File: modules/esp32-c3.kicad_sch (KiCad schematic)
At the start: 26 parts, among them J1 UART0, SW1 BOOT, SW2 RST, U2 ESP32-C3, U3 W25X40CLSN, Y1 40MHz

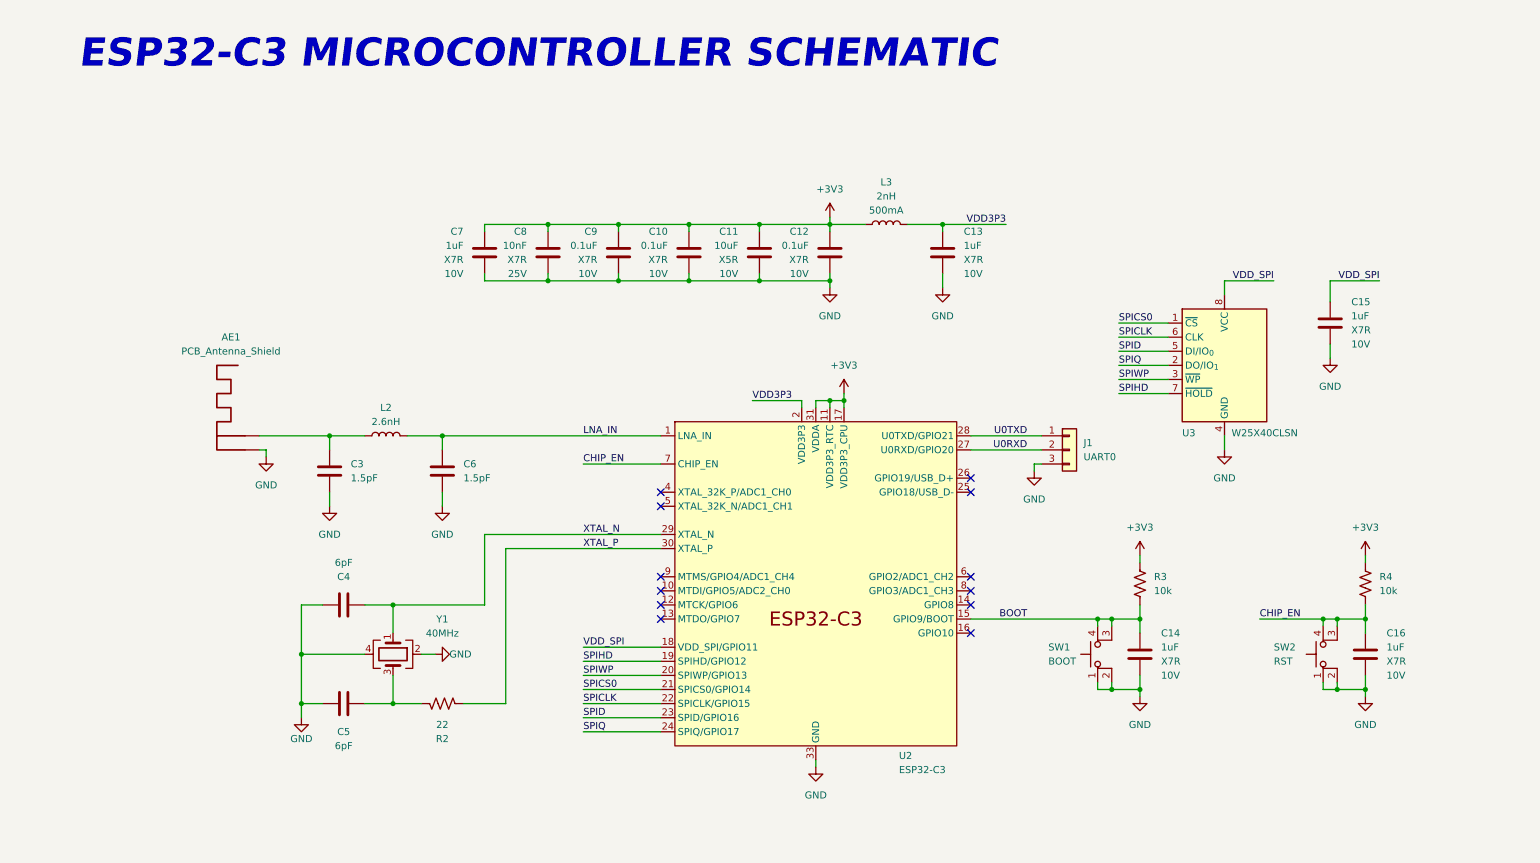
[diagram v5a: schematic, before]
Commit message: Fabrication.kicad_jobset added.
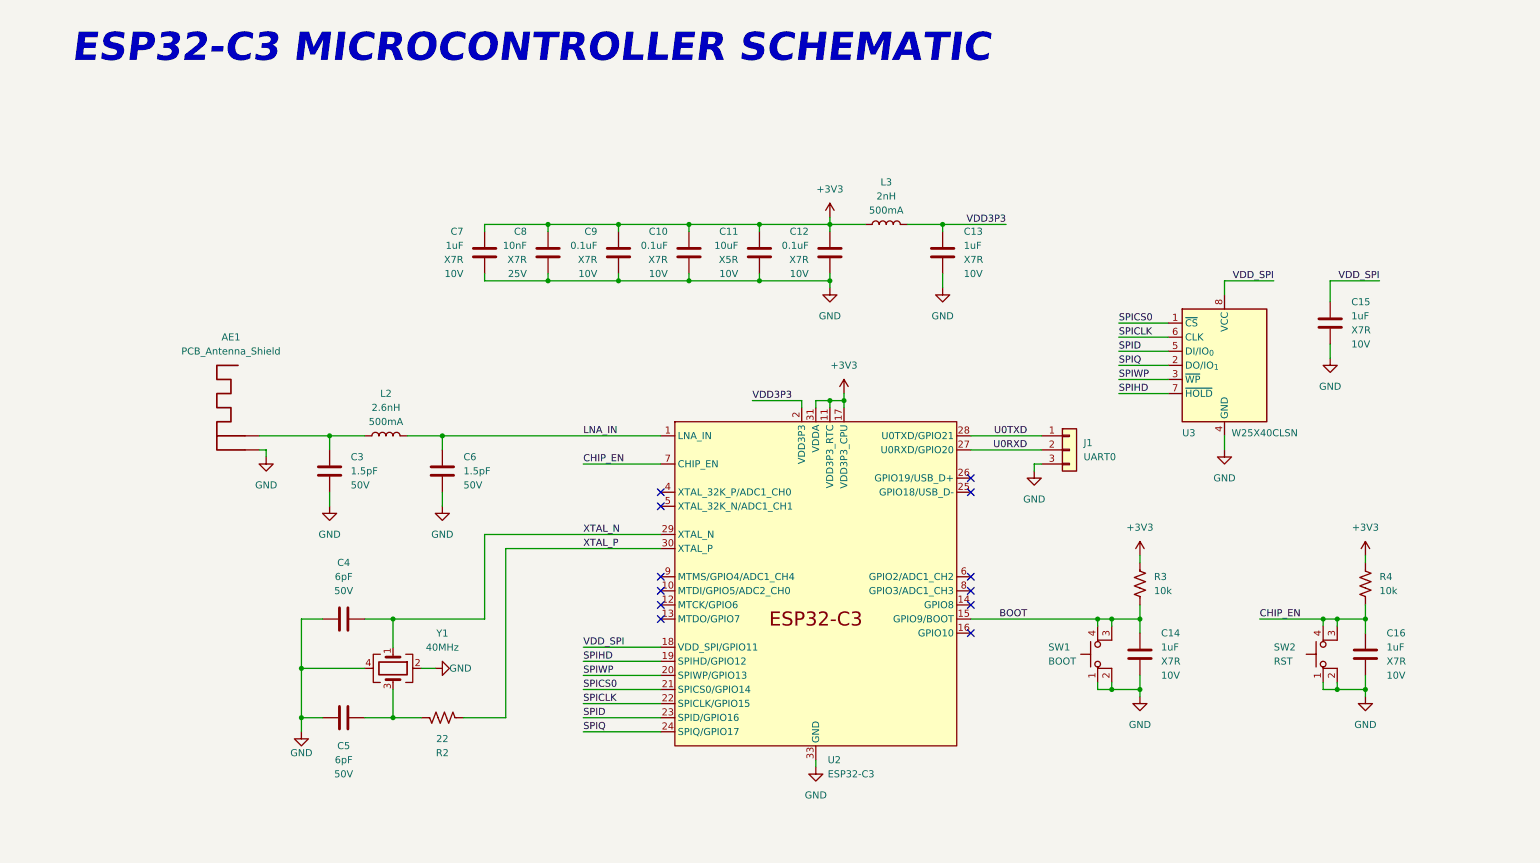
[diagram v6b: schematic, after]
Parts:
- C10, C12, C9: Cost (none) -> 0,00400; Descrip CAP CER 0.1UF 10V X7R 0402 -> (none); PROVIDER Digikey -> (none); Price 0,00400 -> (none); Supplier (none) -> Digikey; VOLTAGE 10V -> (none); Voltage (none) -> 10V
- C11: Cost (none) -> 0,01680; Descrip CAP CER 10UF 10V X5R 0402 -> (none); PROVIDER Digikey -> (none); Price 0,01680 -> (none); Supplier (none) -> Digikey; VOLTAGE 10V -> (none); Voltage (none) -> 10V
- C13, C14, C15, C16, C7: Cost (none) -> 0,01280; Descrip CAP CER 1UF 10V X7R 0402 -> (none); PROVIDER Digikey -> (none); Price 0,01280 -> (none); Supplier (none) -> Digikey; VOLTAGE 10V -> (none); Voltage (none) -> 10V
- C3, C6: Cost (none) -> 0,00398; Descrip CAP CER 1.5PF 50V C0G/NP0 0201 -> (none); PROVIDER Digikey -> (none); Price 0,00398 -> (none); Supplier (none) -> Digikey; VOLTAGE 50V -> (none); Voltage (none) -> 50V
- C4, C5: Cost (none) -> 0,00839; Descrip CAP CER 6PF 50V C0G/NPO 0402 -> (none); PROVIDER Digikey -> (none); Price 0,00839 -> (none); Supplier (none) -> Digikey; VOLTAGE 50V -> (none); Voltage (none) -> 50V
- C8: Cost (none) -> 0,01989; Descrip CAP CER 0402 10NF 25V X7R 10% -> (none); PROVIDER Digikey -> (none); Price 0,01989 -> (none); Supplier (none) -> Digikey; VOLTAGE 25V -> (none); Voltage (none) -> 25V
- L2: CURRENT 500mA -> (none); Cost (none) -> 0,02203; Current (none) -> 500mA; Descrip FIXED IND 2.6NH 500MA 200MOHM SM -> (none); PROVIDER Digikey -> (none); Price 0,02203 -> (none); Supplier (none) -> Digikey
- L3: CURRENT 500mA -> (none); Cost (none) -> 0,03630; Current (none) -> 500mA; Descrip FIXED IND 2NH 500MA 200 MOHM SMD -> (none); PROVIDER Digikey -> (none); Price 0,03630 -> (none); Supplier (none) -> Digikey
- R2: Cost (none) -> 0,00720; Descrip RES SMD 22 OHM 1% 1/10W 0402 -> (none); PROVIDER Digikey -> (none); Price 0,00720 -> (none); Supplier (none) -> Digikey
- R3, R4: Cost (none) -> 0,00720; Descrip RES SMD 10K OHM 1% 1/10W 0402 -> (none); PROVIDER Digikey -> (none); Price 0,00720 -> (none); Supplier (none) -> Digikey
- SW1, SW2: Cost (none) -> 0,11758; Descrip SWITCH TACTILE SPST-NO 0.05A 12V -> (none); PROVIDER Digikey -> (none); Price 0,11758 -> (none); Supplier (none) -> Digikey
- U2: Cost (none) -> 1; Descrip RF TXRX MOD BLUETOOTH WIFISMD -> (none); PROVIDER Digikey -> (none); Price 1 -> (none); Supplier (none) -> Digikey
- U3: Cost (none) -> 0,24624; Descrip IC FLASH 4MBIT SPI 104MHZ 8SOIC -> (none); PROVIDER Digikey -> (none); Price 0,24624 -> (none); Supplier (none) -> Digikey
- Y1: Cost (none) -> 0,12494; Descrip CRYSTAL 40.0000MHZ 6PF SMD -> (none); PROVIDER Digikey -> (none); Price 0,12494 -> (none); Supplier (none) -> Digikey
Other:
- moved on the sheet: C4, C5, R2, Y1
